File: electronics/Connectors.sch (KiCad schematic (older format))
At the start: 35 parts

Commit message: Updated gitignore, switched out regulator
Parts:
- removed ?: LM20323MH_NOPB, MXA20A, symbol LM20323MH_NOPB:LM20323MH_NOPB
- removed C?: 0.1uF, symbol Device:C
- removed C? (x2): 47uF, symbol Device:CP
- removed C?: 6.8nF, symbol Device:C
- removed C?: 10uF, symbol Device:C
- removed C?: 10pF, symbol Device:C
- removed R?: 10k, symbol Device:R
- removed R?: 47k, symbol Device:R
- removed R?: 56k, symbol Device:R
- added C?: 47uF, symbol Device:CP
- added C?: 0.1uF, symbol Device:C
- added C?: 1uF, symbol Device:C
- added C?: 3.3nF, symbol Device:C
- added R?: 22k, symbol Device:R
- added R?: 10k, symbol Device:R
- added U?: TPS54227DDAR, Electronics:TPS54227DDAR, symbol TPS54227DDAR:TPS54227DDAR
- C?: value 6.8nF -> 10pF
- L?: value 10uH -> 4.7uH
- R?: value 7.5k -> 130k
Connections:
- wire segments 64 -> 52
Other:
- moved on the sheet: C?

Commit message: Attached footprints to components
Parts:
- C19, C29: renamed from C?; footprint (none) -> Capacitor_THT:CP_Radial_D8.0mm_P3.50mm
- C20, C21, C22, C23, C24, C26, C27, C28, C30: renamed from C?; footprint (none) -> Capacitor_SMD:C_0603_1608Metric_Pad1.08x0.95mm_HandSolder
- C25: renamed from C?; footprint (none) -> Capacitor_THT:CP_Radial_D5.0mm_P2.00mm
- D5: renamed from D?; footprint (none) -> Diode_SMD:D_0603_1608Metric_Pad1.05x0.95mm_HandSolder
- J10, J11, J12, J7, J8, J9: renamed from J?; footprint TE_215079-4 -> Electronics:TE_215079-4
- J14: renamed from J?; footprint (none) -> Electronics:3mm_pad
- J15: renamed from J?; footprint SAMTEC_FTSH-105-XX-X-DV -> Electronics:SAMTEC_FTSH-105-XX-X-DV
- J16: renamed from J?; footprint FCI_10118193-0001LF -> Electronics:FCI_10118193-0001LF
- L1: renamed from L?; footprint (none) -> Inductor_SMD:L_0603_1608Metric_Pad1.05x0.95mm_HandSolder
- R14, R15, R16, R17: renamed from R?; footprint (none) -> Resistor_SMD:R_0603_1608Metric_Pad0.98x0.95mm_HandSolder
- U10: renamed from U?; footprint (none) -> Electronics:CM1223-02SO
- U9: renamed from U?; footprint (none) -> Electronics:NCP164
- gave numbers to parts that had none: 3

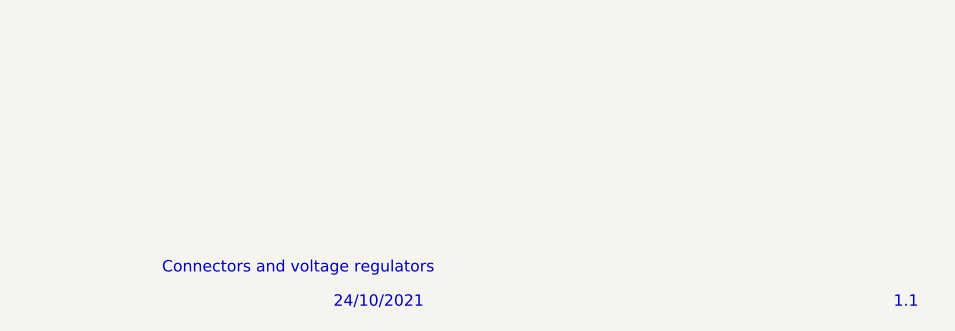
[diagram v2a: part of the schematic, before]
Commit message: Figured out how to automatically change date and revision
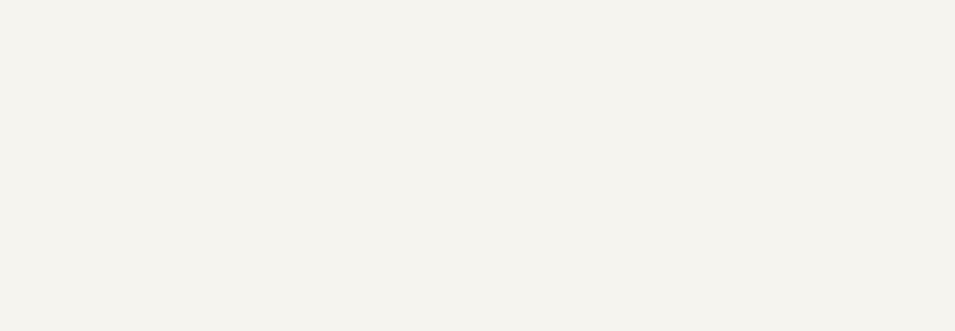
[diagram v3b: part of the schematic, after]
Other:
- note removed: "1.1"
- note removed: "24/10/2021"
- note removed: "Connectors and voltage regulators\n"

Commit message: Relocated items
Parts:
- C19, C29: value 47uF -> 100uF; footprint Capacitor_THT:CP_Radial_D8.0mm_P3.50mm -> Capacitor_SMD:CP_Elec_8x10
- C25: value 4.7uF -> 470uF; footprint Capacitor_THT:CP_Radial_D5.0mm_P2.00mm -> Capacitor_THT:CP_Radial_D10.0mm_P5.00mm
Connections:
- wire segments 52 -> 51
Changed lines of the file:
@@
 AR Path="/617B7795/61AA575E" Ref="C25"  Part="1"
 F 0 "C25" H 6668 4446 50  0000 L CNN
-F 1 "4.7uF" H 6668 4355 50  0000 L CNN
-F 2 "Capacitor_THT:CP_Radial_D5.0mm_P2.00mm" H 6588 4250 50  0001 C CNN
+F 1 "470uF" H 6668 4355 50  0000 L CNN
+F 2 "Capacitor_THT:CP_Radial_D10.0mm_P5.00mm" H 6588 4250 50  0001 C CNN
 F 3 "~" H 6550 4400 50  0001 C CNN
 	1    6550 4400
@@
 AR Path="/617B7795/617815E1" Ref="C19"  Part="1"
 F 0 "C19" H 4433 2646 50  0000 R CNN
-F 1 "47uF" H 4433 2555 50  0000 R CNN
-F 2 "Capacitor_THT:CP_Radial_D8.0mm_P3.50mm" H 4588 2450 50  0001 C CNN
+F 1 "100uF" H 4433 2555 50  0000 R CNN
+F 2 "Capacitor_SMD:CP_Elec_8x10" H 4588 2450 50  0001 C CNN
 F 3 "~" H 4550 2600 50  0001 C CNN
 	1    4550 2600
@@
 AR Path="/617B7795/617CBB79" Ref="C29"  Part="1"
 F 0 "C29" H 8183 2846 50  0000 R CNN
-F 1 "47uF" H 8183 2755 50  0000 R CNN
-F 2 "Capacitor_THT:CP_Radial_D8.0mm_P3.50mm" H 8338 2650 50  0001 C CNN
+F 1 "100uF" H 8183 2755 50  0000 R CNN
+F 2 "Capacitor_SMD:CP_Elec_8x10" H 8338 2650 50  0001 C CNN
 F 3 "~" H 8300 2800 50  0001 C CNN
 	1    8300 2800
@@
 Connection ~ 5000 2450
 Wire Wire Line
-	5000 2450 5200 2450
-Wire Wire Line
 	5500 2650 5600 2650
 Wire Wire Line
@@
 $EndComp
 Wire Wire Line
-	5000 2500 5000 2450
-Wire Wire Line
 	5000 2450 5000 2400
 $Comp
@@
 EndData
 $EndBitmap
+Wire Wire Line
+	5000 2450 5200 2450
 $EndSCHEMATC

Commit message: Updated item locations
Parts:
- L1: footprint Inductor_SMD:L_0603_1608Metric_Pad1.05x0.95mm_HandSolder -> Inductor_SMD:L_7.3x7.3_H4.5
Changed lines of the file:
@@
 F 0 "L1" V 7140 2650 50  0000 C CNN
 F 1 "4.7uH" V 7049 2650 50  0000 C CNN
-F 2 "Inductor_SMD:L_0603_1608Metric_Pad1.05x0.95mm_HandSolder" H 6950 2650 50  0001 C CNN
+F 2 "Inductor_SMD:L_7.3x7.3_H4.5" H 6950 2650 50  0001 C CNN
 F 3 "~" H 6950 2650 50  0001 C CNN
 	1    6950 2650
